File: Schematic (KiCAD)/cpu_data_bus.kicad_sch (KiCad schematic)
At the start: 140 parts, among them P13 INVERT, P19 INVERT, P26 INVERT, P5 INVERT, P7 INVERT, X18 INVERT, X19 INVERT, X20 INVERT, X21 INVERT, X22 INVERT, X23 INVERT, X24 INVERT, X25 INVERT, Y11 INVERT, Y12 INVERT, Y18 INVERT, Y19 INVERT, Y25 INVERT, Y26 INVERT, Y4 INVERT, Y5 INVERT

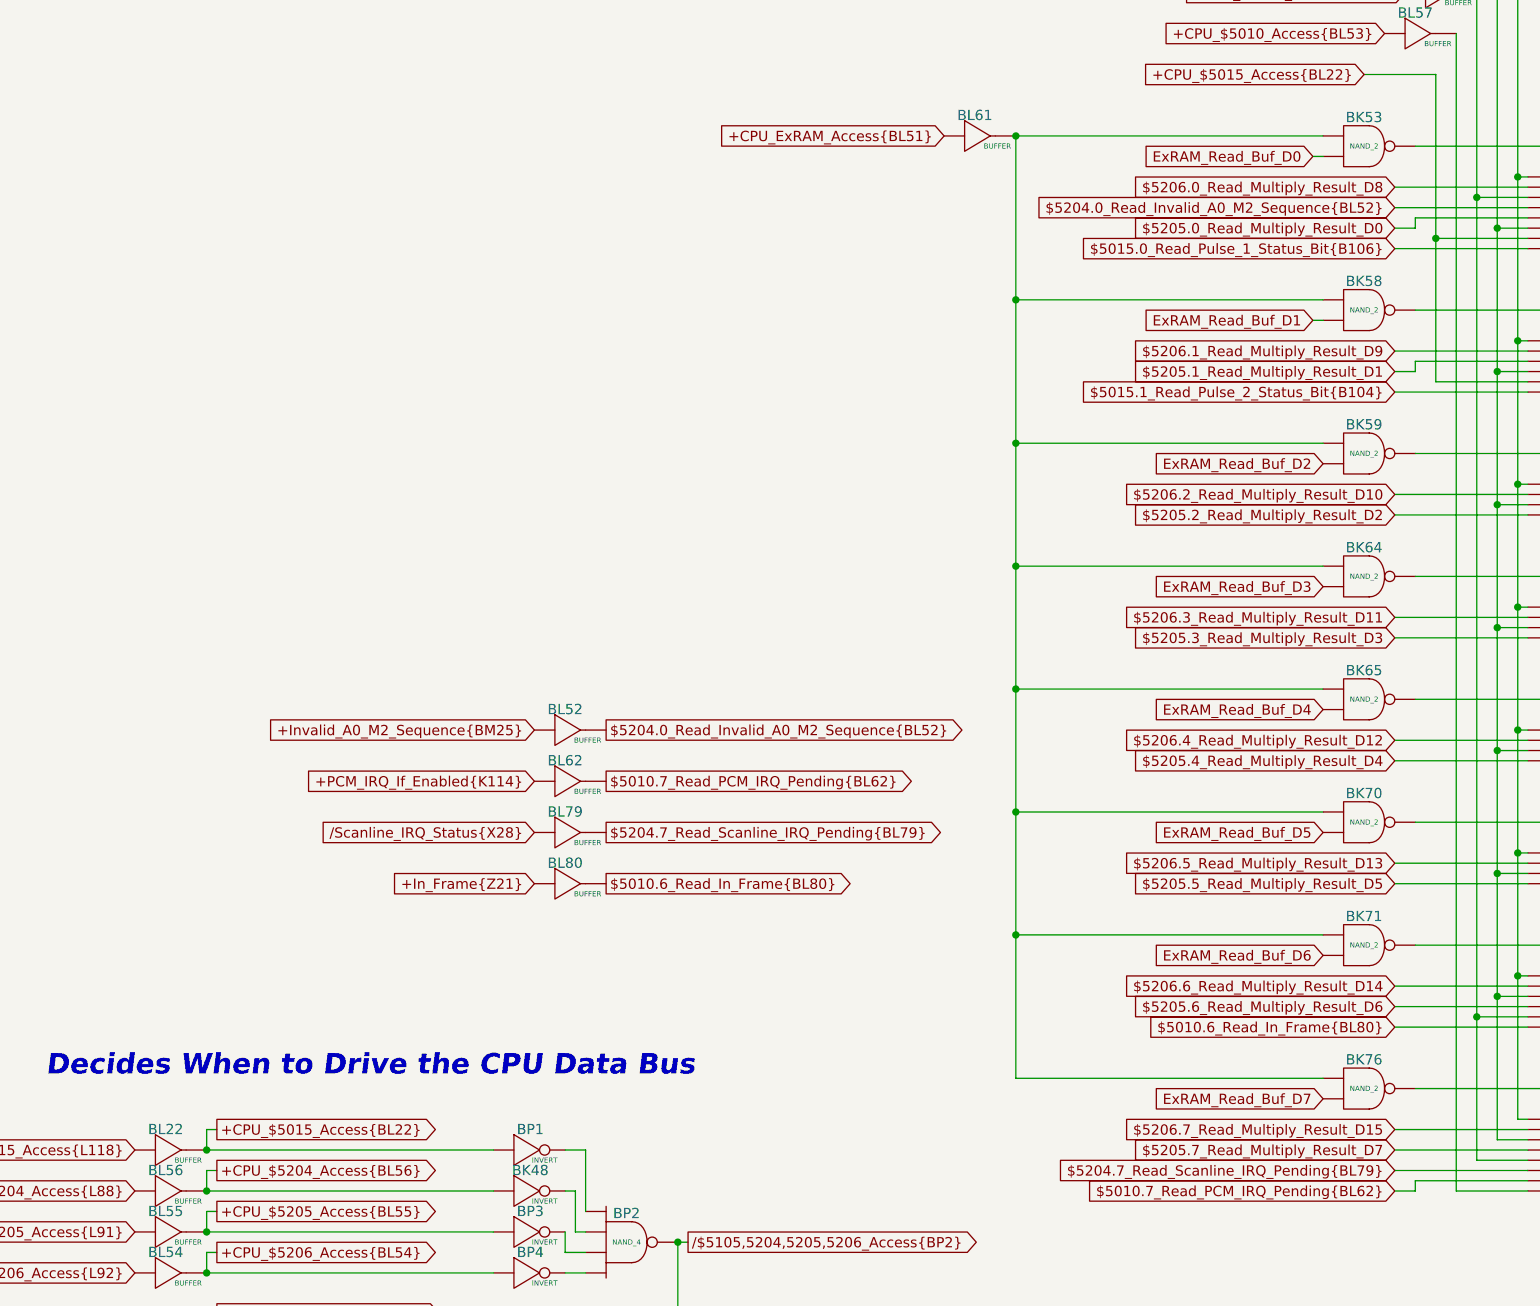
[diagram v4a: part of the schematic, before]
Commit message: - All known gates and traces are now accounted for in the schematics!  :)
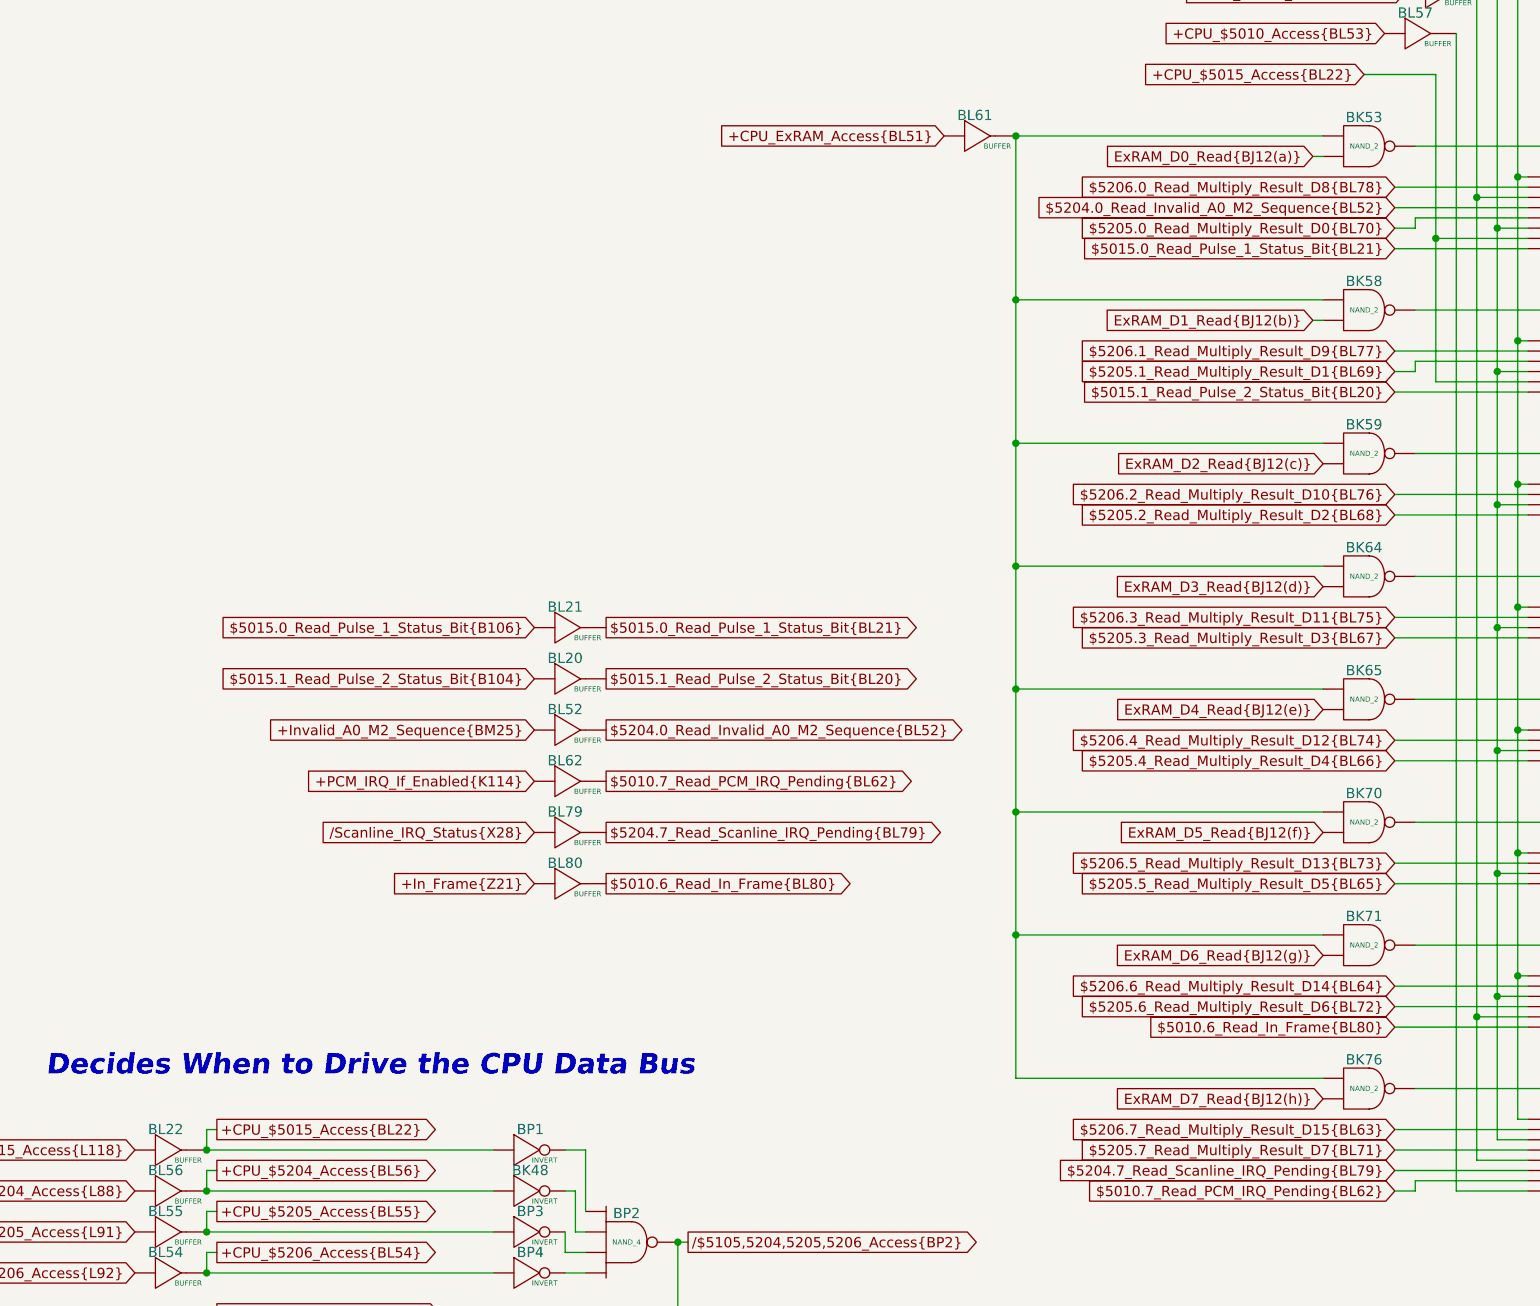
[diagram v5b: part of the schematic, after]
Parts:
- added BL20, BL21: BUFFER, symbol MMC5:BUFFER
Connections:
- net $5205.0_Read_Multiply_Result_D0 is gone; now on net +CPU_$5015_Access{BL22}: BK55. (X)
- net $5205.1_Read_Multiply_Result_D1 is gone; now on net +CPU_$5015_Access{BL22}: BK56. (X)
- net $5205.2_Read_Multiply_Result_D2 is gone; now on net $5206.2_Read_Multiply_Result_D10{BL76}: BK61. (X)
- net $5205.3_Read_Multiply_Result_D3 is gone; now on net $5206.3_Read_Multiply_Result_D11{BL75}: BK62. (X)
- net $5205.4_Read_Multiply_Result_D4 is gone; now on net $5206.4_Read_Multiply_Result_D12{BL74}: BK67. (X)
- net $5205.5_Read_Multiply_Result_D5 is gone; now on net $5206.5_Read_Multiply_Result_D13{BL73}: BK68. (X)
- net $5205.6_Read_Multiply_Result_D6 is gone; now on net $5206.6_Read_Multiply_Result_D14{BL64}: BK73. (X)
- net $5205.7_Read_Multiply_Result_D7 is gone; now on net $5206.7_Read_Multiply_Result_D15{BL63}: BK74. (X)
- net $5206.0_Read_Multiply_Result_D8 is gone; now on net +CPU_$5015_Access{BL22}: BK55. (X)
- net $5206.1_Read_Multiply_Result_D9 is gone; now on net +CPU_$5015_Access{BL22}: BK56. (X)
- net $5206.2_Read_Multiply_Result_D10 is gone; now on net $5206.2_Read_Multiply_Result_D10{BL76}: BK61. (X)
- net $5206.3_Read_Multiply_Result_D11 is gone; now on net $5206.3_Read_Multiply_Result_D11{BL75}: BK62. (X)
- net $5206.4_Read_Multiply_Result_D12 is gone; now on net $5206.4_Read_Multiply_Result_D12{BL74}: BK67. (X)
- net $5206.5_Read_Multiply_Result_D13 is gone; now on net $5206.5_Read_Multiply_Result_D13{BL73}: BK68. (X)
- net $5206.6_Read_Multiply_Result_D14 is gone; now on net $5206.6_Read_Multiply_Result_D14{BL64}: BK73. (X)
- net $5206.7_Read_Multiply_Result_D15 is gone; now on net $5206.7_Read_Multiply_Result_D15{BL63}: BK74. (X)
- net ExRAM_Read_Buf_D0 is gone; now on net ExRAM_D0_Read{BJ12(a)}: BK53. (X)
- net ExRAM_Read_Buf_D1 is gone; now on net ExRAM_D1_Read{BJ12(b)}: BK58. (X)
- net ExRAM_Read_Buf_D2 is gone; now on net ExRAM_D2_Read{BJ12(c)}: BK59. (X)
- net ExRAM_Read_Buf_D3 is gone; now on net ExRAM_D3_Read{BJ12(d)}: BK64. (X)
- net ExRAM_Read_Buf_D4 is gone; now on net ExRAM_D4_Read{BJ12(e)}: BK65. (X)
- net ExRAM_Read_Buf_D5 is gone; now on net ExRAM_D5_Read{BJ12(f)}: BK70. (X)
- net ExRAM_Read_Buf_D6 is gone; now on net ExRAM_D6_Read{BJ12(g)}: BK71. (X)
- net ExRAM_Read_Buf_D7 is gone; now on net ExRAM_D7_Read{BJ12(h)}: BK76. (X)
- net $5015.0_Read_Pulse_1_Status_Bit{B106}: now also BL21. (X); no longer BK55. (X)
- net $5015.1_Read_Pulse_2_Status_Bit{B104}: now also BL20. (X); no longer BK56. (X)
- net $5206.4_Read_Multiply_Result_D12{BL74}: now reaches BK67. (X)
- net $5206.4_Read_Multiply_Result_D12{BL74}: no longer BK66. (X)
- net ExRAM_D3_Read{BJ12(d)}: now reaches BK64. (X)
- net ExRAM_D3_Read{BJ12(d)}: no longer BK63. (X)
- net ExRAM_D5_Read{BJ12(f)}: now reaches BK70. (X)
- net ExRAM_D5_Read{BJ12(f)}: no longer BK69. (X)
- net $5206.5_Read_Multiply_Result_D13{BL73}: now reaches BK68. (X)
- net $5206.5_Read_Multiply_Result_D13{BL73}: no longer BK69. (X)
- net ExRAM_D4_Read{BJ12(e)}: now reaches BK65. (X)
- net ExRAM_D4_Read{BJ12(e)}: no longer BK66. (X)
- net ExRAM_D1_Read{BJ12(b)}: now reaches BK58. (X)
- net ExRAM_D1_Read{BJ12(b)}: no longer BK57. (X)
- net ExRAM_D7_Read{BJ12(h)}: now reaches BK76. (X)
- net ExRAM_D7_Read{BJ12(h)}: no longer BK75. (X)
- net at BK47. (X): now also BK46. (X); no longer BL50. (X)
- net ExRAM_D0_Read{BJ12(a)}: now reaches BK53. (X)
- net ExRAM_D0_Read{BJ12(a)}: no longer BK54. (X)
- net $5206.6_Read_Multiply_Result_D14{BL64}: now reaches BK73. (X)
- net $5206.6_Read_Multiply_Result_D14{BL64}: no longer BK72. (X)
- net ExRAM_D6_Read{BJ12(g)}: now reaches BK71. (X)
- net ExRAM_D6_Read{BJ12(g)}: no longer BK72. (X)
- net $5206.7_Read_Multiply_Result_D15{BL63}: now reaches BK74. (X)
- net $5206.7_Read_Multiply_Result_D15{BL63}: no longer BK75. (X)
- net $5206.2_Read_Multiply_Result_D10{BL76}: now reaches BK61. (X)
- net $5206.2_Read_Multiply_Result_D10{BL76}: no longer BK60. (X)
- net ExRAM_D2_Read{BJ12(c)}: now reaches BK59. (X)
- net ExRAM_D2_Read{BJ12(c)}: no longer BK60. (X)
- net $5206.3_Read_Multiply_Result_D11{BL75}: now reaches BK62. (X)
- net $5206.3_Read_Multiply_Result_D11{BL75}: no longer BK63. (X)
- net at BK51. (X): now also BK49. (X); no longer BK52. (X)
- new net: BK55. (X), BK56. (X), BK61. (X), BK62. (X), BK67. (X), BK68. (X), BK73. (X), BK74. (X), BL58. (X)
- new net: BK55. (X), BK56. (X), BK61. (X), BK62. (X), BK67. (X), BK68. (X), BK73. (X), BK74. (X), BL59. (X)
- new net: BK66. (X), BK67. (X)
- new net: BK53. (X), BK58. (X), BK59. (X), BK64. (X), BK65. (X), BK70. (X), BK71. (X), BK76. (X), BL61. (X)
- new net: BK63. (X), BK64. (X)
- new net: BK69. (X), BK70. (X)
- new net: BK68. (X), BK69. (X)
- new net: BK65. (X), BK66. (X)
- new net: BK57. (X), BK58. (X)
- new net: G15. (X), G16. (X)
- new net: BK75. (X), BK76. (X)
- new net: G10. (X), G9. (X)
- new net: AE15. (X), AE19. (X), G13. (X), MUL20. (X), X19. (X)
- new net: BK47. (X), BL50. (X)
- new net: G1. (X), G2. (X)
- new net: G7. (X), G8. (X)
- new net: G11. (X), G12. (X)
- new net: G5. (X), G6. (X)
- new net: BK53. (X), BK54. (X)
- new net: G3. (X), G4. (X)
- new net: BK48. (X), BP2. (X)
- new net: BP2. (X), BP3. (X)
- new net: BK55. (X), BK73. (X), BK74. (X), BL60. (X)
- new net: BK54. (X), BK55. (X)
- new net: BK72. (X), BK73. (X)
- new net: BK71. (X), BK72. (X)
- new net: BK74. (X), BK75. (X)
- new net: BK74. (X), BL57. (X)
- new net: BK60. (X), BK61. (X)
- new net: BK59. (X), BK60. (X)
- new net: BK56. (X), BK57. (X)
- new net: BK62. (X), BK63. (X)
- new net: BK51. (X), BK52. (X)
- new net: BP1. (X), BP2. (X)
- new net: BK50. (X), BK51. (X)
- new net: BK46. (X), BK51. (X)
- new net: BP2. (X), BP4. (X)
- new net: BK45. (X), BK46. (X)
- new net $5015.0_Read_Pulse_1_Status_Bit{BL21}: BK55. (X), BL21. (X)
- new net $5015.1_Read_Pulse_2_Status_Bit{BL20}: BK56. (X), BL20. (X)
- new net $5205.0_Read_Multiply_Result_D0{BL70}: BK55. (X)
- new net $5205.1_Read_Multiply_Result_D1{BL69}: BK56. (X)
- new net $5205.2_Read_Multiply_Result_D2{BL68}: BK61. (X)
- new net $5205.3_Read_Multiply_Result_D3{BL67}: BK62. (X)
- new net $5205.4_Read_Multiply_Result_D4{BL66}: BK67. (X)
- new net $5205.5_Read_Multiply_Result_D5{BL65}: BK68. (X)
- new net $5205.6_Read_Multiply_Result_D6{BL72}: BK73. (X)
- new net $5205.7_Read_Multiply_Result_D7{BL71}: BK74. (X)
- new net $5206.0_Read_Multiply_Result_D8{BL78}: BK55. (X)
- new net $5206.1_Read_Multiply_Result_D9{BL77}: BK56. (X)
